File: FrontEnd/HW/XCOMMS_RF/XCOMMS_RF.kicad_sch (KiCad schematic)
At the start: 60 parts, among them J1 SMP-MSLD-PCE-5T, J2 SMP-MSLD-PCE-5T, J3 SFC-110-T2-F-D-A-TR, U1 SIM-14+, U2 HMC788ALP2ETR, U3 HMC952ALP5GE, U5 HMC788ALP2ETR, U6 AD8031, U7 ADT7310, U8 HMC788ALP2ETR

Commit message: XCOMMS Interface rebuild
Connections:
- net +5V renamed Vdd_AMP
- net Vd_PA renamed Vdd_PA
- no-connect marks 0 -> 2
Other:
- note added: "Connectors"
- note added: "Screws"
- note removed: "Alternative 2"
- note removed: "Connectors and Screws"
- note removed: "IC | V (V) | I (mA) | Power (mW) - - - - - - - - - - - - - - - - - - - PA | 6 | 1400 | ~2500 (class C) AMP1 | 5 | 56 | 280 HMC311LP3 AMP2 | 5 | 43 | 21 HMC3587LP3BE VCO | 2.75 | 80 | 220 - - - - - - - - - - - - - - - - - - - Total | 3.2 W Notes: SDR output @ 2 GHz"
- moved on the sheet: C10, C11, C12, C15, C16, C17, C18, C19, C20, C23, C24, C25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

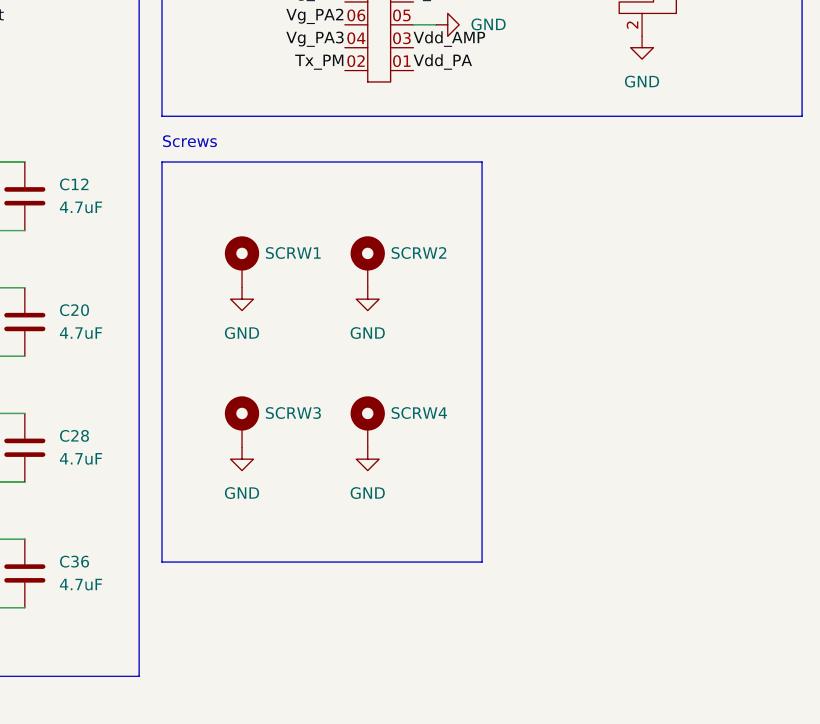
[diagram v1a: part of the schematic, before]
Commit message: xtal changed and routing
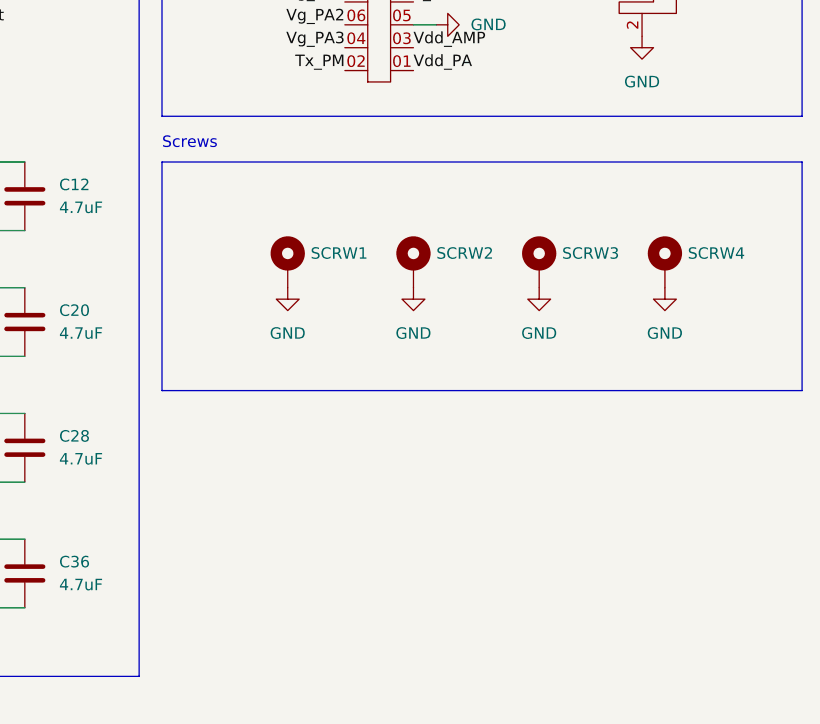
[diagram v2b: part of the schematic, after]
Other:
- moved on the sheet: SCRW1, SCRW2, SCRW3, SCRW4
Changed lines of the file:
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@@
     (stroke (width 0) (type default) (color 0 0 0 0))
   )
-  (polyline (pts (xy 210.82 107.95) (xy 246.38 107.95))
+  (polyline (pts (xy 210.82 107.95) (xy 281.94 107.95))
     (stroke (width 0) (type default) (color 0 0 0 0))
   )
@@
     (stroke (width 0) (type default) (color 0 0 0 0))
   )
-  (polyline (pts (xy 210.82 152.4) (xy 246.38 152.4))
+  (polyline (pts (xy 210.82 133.35) (xy 281.94 133.35))
     (stroke (width 0) (type default) (color 0 0 0 0))
   )
@@
     (stroke (width 0) (type default) (color 0 0 0 0))
   )
-  (polyline (pts (xy 210.82 107.95) (xy 210.82 152.4))
+  (polyline (pts (xy 210.82 107.95) (xy 210.82 133.35))
     (stroke (width 0) (type default) (color 0 0 0 0))
   )
@@
     (stroke (width 0) (type default) (color 0 0 0 0))
   )
-  (polyline (pts (xy 246.38 152.4) (xy 246.38 107.95))
+  (polyline (pts (xy 281.94 133.35) (xy 281.94 107.95))
     (stroke (width 0) (type default) (color 0 0 0 0))
   )
@@
     (pin "1")
   )
-  (symbol (lib_id "Mechanical:MountingHole_Pad") (at 233.68 137.16 0) (unit 1)
+  (symbol (lib_id "Mechanical:MountingHole_Pad") (at 266.7 119.38 0) (unit 1)
     (in_bom yes) (on_board yes) (fields_autoplaced)
-    (property "Reference" "SCRW4" (id 0) (at 236.22 135.8899 0)
+    (property "Reference" "SCRW4" (id 0) (at 269.24 118.1099 0)
       (effects (font (size 1.27 1.27)) (justify left))
     )
-    (property "Value" "MountingHole_Pad" (id 1) (at 233.68 130.81 0)
+    (property "Value" "MountingHole_Pad" (id 1) (at 266.7 113.03 0)
       (effects (font (size 1.27 1.27)) hide)
     )
-    (property "Footprint" "MountingHole:MountingHole_2.7mm_M2.5_ISO14580_Pad" (id 2) (at 233.68 137.16 0)
+    (property "Footprint" "MountingHole:MountingHole_2.7mm_M2.5_ISO14580_Pad" (id 2) (at 266.7 119.38 0)
       (effects (font (size 1.27 1.27)) hide)
     )
-    (property "Datasheet" "~" (id 3) (at 233.68 137.16 0)
+    (property "Datasheet" "~" (id 3) (at 266.7 119.38 0)
       (effects (font (size 1.27 1.27)) hide)
     )
@@
     (pin "2")
   )
-  (symbol (lib_id "power:GND") (at 233.68 139.7 0) (unit 1)
+  (symbol (lib_id "power:GND") (at 266.7 121.92 0) (unit 1)
     (in_bom yes) (on_board yes) (fields_autoplaced)
-    (property "Reference" "#PWR0103" (id 0) (at 233.68 146.05 0)
+    (property "Reference" "#PWR0103" (id 0) (at 266.7 128.27 0)
       (effects (font (size 1.27 1.27)) hide)
     )
-    (property "Value" "GND" (id 1) (at 233.68 144.78 0))
-    (property "Footprint" "" (id 2) (at 233.68 139.7 0)
+    (property "Value" "GND" (id 1) (at 266.7 127 0))
+    (property "Footprint" "" (id 2) (at 266.7 121.92 0)
       (effects (font (size 1.27 1.27)) hide)
     )
-    (property "Datasheet" "" (id 3) (at 233.68 139.7 0)
+    (property "Datasheet" "" (id 3) (at 266.7 121.92 0)
       (effects (font (size 1.27 1.27)) hide)
     )
@@
     (pin "1")
   )
-  (symbol (lib_id "Mechanical:MountingHole_Pad") (at 219.71 137.16 0) (unit 1)
+  (symbol (lib_id "Mechanical:MountingHole_Pad") (at 252.73 119.38 0) (unit 1)
     (in_bom yes) (on_board yes) (fields_autoplaced)
-    (property "Reference" "SCRW3" (id 0) (at 222.25 135.8899 0)
+    (property "Reference" "SCRW3" (id 0) (at 255.27 118.1099 0)
       (effects (font (size 1.27 1.27)) (justify left))
     )
-    (property "Value" "MountingHole_Pad" (id 1) (at 222.25 137.1599 0)
+    (property "Value" "MountingHole_Pad" (id 1) (at 255.27 119.3799 0)
       (effects (font (size 1.27 1.27)) (justify left) hide)
     )
-    (property "Footprint" "MountingHole:MountingHole_2.7mm_M2.5_ISO14580_Pad" (id 2) (at 219.71 137.16 0)
+    (property "Footprint" "MountingHole:MountingHole_2.7mm_M2.5_ISO14580_Pad" (id 2) (at 252.73 119.38 0)
       (effects (font (size 1.27 1.27)) hide)
     )
-    (property "Datasheet" "~" (id 3) (at 219.71 137.16 0)
+    (property "Datasheet" "~" (id 3) (at 252.73 119.38 0)
       (effects (font (size 1.27 1.27)) hide)
     )
@@
     (pin "1")
   )
-  (symbol (lib_id "Mechanical:MountingHole_Pad") (at 233.68 119.38 0) (unit 1)
+  (symbol (lib_id "Mechanical:MountingHole_Pad") (at 238.76 119.38 0) (unit 1)
     (in_bom yes) (on_board yes) (fields_autoplaced)
-    (property "Reference" "SCRW2" (id 0) (at 236.22 118.1099 0)
+    (property "Reference" "SCRW2" (id 0) (at 241.3 118.1099 0)
       (effects (font (size 1.27 1.27)) (justify left))
     )
-    (property "Value" "MountingHole_Pad" (id 1) (at 233.68 113.03 0)
+    (property "Value" "MountingHole_Pad" (id 1) (at 238.76 113.03 0)
       (effects (font (size 1.27 1.27)) hide)
     )
-    (property "Footprint" "MountingHole:MountingHole_2.7mm_M2.5_ISO14580_Pad" (id 2) (at 233.68 119.38 0)
+    (property "Footprint" "MountingHole:MountingHole_2.7mm_M2.5_ISO14580_Pad" (id 2) (at 238.76 119.38 0)
       (effects (font (size 1.27 1.27)) hide)
     )
-    (property "Datasheet" "~" (id 3) (at 233.68 119.38 0)
+    (property "Datasheet" "~" (id 3) (at 238.76 119.38 0)
       (effects (font (size 1.27 1.27)) hide)
     )
@@
     (pin "1")
   )
-  (symbol (lib_id "power:GND") (at 233.68 121.92 0) (unit 1)
+  (symbol (lib_id "power:GND") (at 238.76 121.92 0) (unit 1)
     (in_bom yes) (on_board yes) (fields_autoplaced)
-    (property "Reference" "#PWR0113" (id 0) (at 233.68 128.27 0)
+    (property "Reference" "#PWR0113" (id 0) (at 238.76 128.27 0)
       (effects (font (size 1.27 1.27)) hide)
     )
-    (property "Value" "GND" (id 1) (at 233.68 127 0))
-    (property "Footprint" "" (id 2) (at 233.68 121.92 0)
+    (property "Value" "GND" (id 1) (at 238.76 127 0))
+    (property "Footprint" "" (id 2) (at 238.76 121.92 0)
       (effects (font (size 1.27 1.27)) hide)
     )
-    (property "Datasheet" "" (id 3) (at 233.68 121.92 0)
+    (property "Datasheet" "" (id 3) (at 238.76 121.92 0)
       (effects (font (size 1.27 1.27)) hide)
     )
@@
     (pin "2")
   )
-  (symbol (lib_id "Mechanical:MountingHole_Pad") (at 219.71 119.38 0) (unit 1)
+  (symbol (lib_id "Mechanical:MountingHole_Pad") (at 224.79 119.38 0) (unit 1)
     (in_bom yes) (on_board yes) (fields_autoplaced)
-    (property "Reference" "SCRW1" (id 0) (at 222.25 118.1099 0)
+    (property "Reference" "SCRW1" (id 0) (at 227.33 118.1099 0)
       (effects (font (size 1.27 1.27)) (justify left))
     )
-    (property "Value" "MountingHole_Pad" (id 1) (at 222.25 119.3799 0)
+    (property "Value" "MountingHole_Pad" (id 1) (at 227.33 119.3799 0)
       (effects (font (size 1.27 1.27)) (justify left) hide)
     )
-    (property "Footprint" "MountingHole:MountingHole_2.7mm_M2.5_ISO14580_Pad" (id 2) (at 219.71 119.38 0)
+    (property "Footprint" "MountingHole:MountingHole_2.7mm_M2.5_ISO14580_Pad" (id 2) (at 224.79 119.38 0)
       (effects (font (size 1.27 1.27)) hide)
     )
-    (property "Datasheet" "~" (id 3) (at 219.71 119.38 0)
+    (property "Datasheet" "~" (id 3) (at 224.79 119.38 0)
       (effects (font (size 1.27 1.27)) hide)
     )
@@
     (pin "1")
   )
-  (symbol (lib_id "power:GND") (at 219.71 121.92 0) (unit 1)
+  (symbol (lib_id "power:GND") (at 224.79 121.92 0) (unit 1)
     (in_bom yes) (on_board yes) (fields_autoplaced)
-    (property "Reference" "#PWR0114" (id 0) (at 219.71 128.27 0)
+    (property "Reference" "#PWR0114" (id 0) (at 224.79 128.27 0)
       (effects (font (size 1.27 1.27)) hide)
     )
-    (property "Value" "GND" (id 1) (at 219.71 127 0))
-    (property "Footprint" "" (id 2) (at 219.71 121.92 0)
+    (property "Value" "GND" (id 1) (at 224.79 127 0))
+    (property "Footprint" "" (id 2) (at 224.79 121.92 0)
       (effects (font (size 1.27 1.27)) hide)
     )
-    (property "Datasheet" "" (id 3) (at 219.71 121.92 0)
+    (property "Datasheet" "" (id 3) (at 224.79 121.92 0)
       (effects (font (size 1.27 1.27)) hide)
     )
@@
     (pin "1")
   )
-  (symbol (lib_id "power:GND") (at 219.71 139.7 0) (unit 1)
+  (symbol (lib_id "power:GND") (at 252.73 121.92 0) (unit 1)
     (in_bom yes) (on_board yes) (fields_autoplaced)
-    (property "Reference" "#PWR0106" (id 0) (at 219.71 146.05 0)
+    (property "Reference" "#PWR0106" (id 0) (at 252.73 128.27 0)
       (effects (font (size 1.27 1.27)) hide)
     )
-    (property "Value" "GND" (id 1) (at 219.71 144.78 0))
-    (property "Footprint" "" (id 2) (at 219.71 139.7 0)
+    (property "Value" "GND" (id 1) (at 252.73 127 0))
+    (property "Footprint" "" (id 2) (at 252.73 121.92 0)
       (effects (font (size 1.27 1.27)) hide)
     )
-    (property "Datasheet" "" (id 3) (at 219.71 139.7 0)
+    (property "Datasheet" "" (id 3) (at 252.73 121.92 0)
       (effects (font (size 1.27 1.27)) hide)
     )

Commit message: XCOMMS RF
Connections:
- net GND: now also J3.08; no longer J3.18, J3.20
- net SCK: now also J3.17; no longer J3.15
- net SDI: now also J3.20; no longer J3.19
- net SDO: now also J3.19; no longer J3.17
- net Tx_PM: now also J3.18; no longer J3.02
- net Vg_PA1: now also J3.06; no longer J3.08
- net Vg_PA2: now also J3.04; no longer J3.06
- net Vg_PA3: now also J3.02; no longer J3.04
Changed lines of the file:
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@@
   (junction (at 96.52 143.51) (diameter 0) (color 0 0 0 0)
   )
-  (junction (at 231.14 80.01) (diameter 0) (color 0 0 0 0)
-  )
   (junction (at 49.53 33.02) (diameter 0) (color 0 0 0 0)
   )
@@
   )
   (junction (at 26.67 33.02) (diameter 0) (color 0 0 0 0)
-  )
-  (junction (at 231.14 77.47) (diameter 0) (color 0 0 0 0)
   )
   (junction (at 182.88 107.95) (diameter 0) (color 0 0 0 0)
@@
     (stroke (width 0) (type default) (color 0 0 0 0))
   )
-  (wire (pts (xy 231.14 77.47) (xy 231.14 80.01))
-    (stroke (width 0) (type default) (color 0 0 0 0))
-  )
   (wire (pts (xy 241.3 92.71) (xy 238.76 92.71))
     (stroke (width 0) (type default) (color 0 0 0 0))
@@
     (stroke (width 0) (type default) (color 0 0 0 0))
   )
+  (wire (pts (xy 231.14 87.63) (xy 231.14 90.17))
+    (stroke (width 0) (type default) (color 0 0 0 0))
+  )
   (wire (pts (xy 109.22 41.91) (xy 109.22 39.37))
     (stroke (width 0) (type default) (color 0 0 0 0))
   )
   (wire (pts (xy 252.73 73.66) (xy 259.08 73.66))
-    (stroke (width 0) (type default) (color 0 0 0 0))
-  )
-  (wire (pts (xy 231.14 74.93) (xy 231.14 77.47))
     (stroke (width 0) (type default) (color 0 0 0 0))
   )
@@
     (effects (font (size 1.27 1.27)) (justify left bottom))
   )
-  (label "SDI" (at 238.76 74.93 0)
-    (effects (font (size 1.27 1.27)) (justify left bottom))
-  )
   (label "Vdd_AMP" (at 223.52 45.72 0)
     (effects (font (size 1.27 1.27)) (justify left bottom))
@@
     (effects (font (size 1.27 1.27)) (justify left bottom))
   )
-  (label "Vg_PA3" (at 231.14 95.25 180)
+  (label "RF_In" (at 19.05 27.94 0)
+    (effects (font (size 1.27 1.27)) (justify left bottom))
+  )
+  (label "PLL_CSB" (at 21.59 86.36 0)
+    (effects (font (size 1.27 1.27)) (justify left bottom))
+  )
+  (label "Vdd_PA" (at 158.75 73.66 90)
+    (effects (font (size 1.27 1.27)) (justify left bottom))
+  )
+  (label "SDO" (at 238.76 74.93 0)
+    (effects (font (size 1.27 1.27)) (justify left bottom))
+  )
+  (label "RF_out" (at 189.23 88.9 0)
+    (effects (font (size 1.27 1.27)) (justify left bottom))
+  )
+  (label "Vdd_PA" (at 163.83 73.66 90)
+    (effects (font (size 1.27 1.27)) (justify left bottom))
+  )
+  (label "Vdet" (at 189.23 92.71 0)
+    (effects (font (size 1.27 1.27)) (justify left bottom))
+  )
+  (label "PLL_CE" (at 238.76 87.63 0)
+    (effects (font (size 1.27 1.27)) (justify left bottom))
+  )
+  (label "Vg_PA2" (at 172.72 73.66 90)
+    (effects (font (size 1.27 1.27)) (justify left bottom))
+  )
+  (label "FL_Out" (at 151.13 31.75 0)
+    (effects (font (size 1.27 1.27)) (justify left bottom))
+  )
+  (label "PLL_CSB" (at 238.76 82.55 0)
+    (effects (font (size 1.27 1.27)) (justify left bottom))
+  )
+  (label "Vdd_PA" (at 166.37 73.66 90)
+    (effects (font (size 1.27 1.27)) (justify left bottom))
+  )
+  (label "AMP3_Out" (at 78.74 76.2 0)
+    (effects (font (size 1.27 1.27)) (justify left bottom))
+  )
+  (label "Vdd_PA" (at 172.72 107.95 0)
+    (effects (font (size 1.27 1.27)) (justify left bottom))
+  )
+  (label "PA_RF_IN" (at 137.16 88.9 0)
+    (effects (font (size 1.27 1.27)) (justify left bottom))
+  )
+  (label "AMP2_Out" (at 232.41 27.94 0)
+    (effects (font (size 1.27 1.27)) (justify left bottom))
+  )
+  (label "Vdd_AMP" (at 73.66 125.73 0)
+    (effects (font (size 1.27 1.27)) (justify left bottom))
+  )
+  (label "Vdd_AMP" (at 86.36 125.73 0)
+    (effects (font (size 1.27 1.27)) (justify left bottom))
+  )
+  (label "SCK" (at 238.76 77.47 0)
+    (effects (font (size 1.27 1.27)) (justify left bottom))
+  )
+  (label "Vg_PA3" (at 231.14 97.79 180)
     (effects (font (size 1.27 1.27)) (justify right bottom))
   )
-  (label "RF_In" (at 19.05 27.94 0)
-    (effects (font (size 1.27 1.27)) (justify left bottom))
-  )
-  (label "PLL_CSB" (at 21.59 86.36 0)
-    (effects (font (size 1.27 1.27)) (justify left bottom))
-  )
-  (label "Vdd_PA" (at 158.75 73.66 90)
-    (effects (font (size 1.27 1.27)) (justify left bottom))
-  )
-  (label "RF_out" (at 189.23 88.9 0)
-    (effects (font (size 1.27 1.27)) (justify left bottom))
-  )
-  (label "Vdd_PA" (at 163.83 73.66 90)
-    (effects (font (size 1.27 1.27)) (justify left bottom))
-  )
-  (label "Vdet" (at 189.23 92.71 0)
-    (effects (font (size 1.27 1.27)) (justify left bottom))
-  )
-  (label "PLL_CE" (at 238.76 87.63 0)
-    (effects (font (size 1.27 1.27)) (justify left bottom))
-  )
-  (label "Vg_PA2" (at 172.72 73.66 90)
-    (effects (font (size 1.27 1.27)) (justify left bottom))
-  )
-  (label "FL_Out" (at 151.13 31.75 0)
-    (effects (font (size 1.27 1.27)) (justify left bottom))
-  )
-  (label "PLL_CSB" (at 238.76 82.55 0)
-    (effects (font (size 1.27 1.27)) (justify left bottom))
-  )
-  (label "Vdd_PA" (at 166.37 73.66 90)
-    (effects (font (size 1.27 1.27)) (justify left bottom))
-  )
-  (label "AMP3_Out" (at 78.74 76.2 0)
-    (effects (font (size 1.27 1.27)) (justify left bottom))
-  )
-  (label "Vdd_PA" (at 172.72 107.95 0)
-    (effects (font (size 1.27 1.27)) (justify left bottom))
-  )
-  (label "PA_RF_IN" (at 137.16 88.9 0)
-    (effects (font (size 1.27 1.27)) (justify left bottom))
-  )
-  (label "AMP2_Out" (at 232.41 27.94 0)
-    (effects (font (size 1.27 1.27)) (justify left bottom))
-  )
-  (label "Vdd_AMP" (at 73.66 125.73 0)
-    (effects (font (size 1.27 1.27)) (justify left bottom))
-  )
-  (label "Vdd_AMP" (at 86.36 125.73 0)
-    (effects (font (size 1.27 1.27)) (justify left bottom))
+  (label "Tx_PM" (at 231.14 77.47 180)
+    (effects (font (size 1.27 1.27)) (justify right bottom))
   )
   (label "Vg_PA1" (at 170.18 73.66 90)
@@
     (effects (font (size 1.27 1.27)) (justify left bottom))
   )
-  (label "Tx_PM" (at 231.14 97.79 180)
+  (label "SDI" (at 231.14 74.93 180)
     (effects (font (size 1.27 1.27)) (justify right bottom))
   )
-  (label "Vg_PA1" (at 231.14 90.17 180)
+  (label "Vg_PA1" (at 231.14 92.71 180)
     (effects (font (size 1.27 1.27)) (justify right bottom))
   )
@@
     (effects (font (size 1.27 1.27)) (justify left bottom))
   )
-  (label "SCK" (at 238.76 80.01 0)
-    (effects (font (size 1.27 1.27)) (justify left bottom))
-  )
   (label "RF_out" (at 252.73 73.66 0)
     (effects (font (size 1.27 1.27)) (justify left bottom))
@@
     (effects (font (size 1.27 1.27)) (justify left bottom))
   )
-  (label "SDO" (at 238.76 77.47 0)
-    (effects (font (size 1.27 1.27)) (justify left bottom))
-  )
   (label "Vdd_AMP" (at 238.76 95.25 0)
     (effects (font (size 1.27 1.27)) (justify left bottom))
@@
     (effects (font (size 1.27 1.27)) (justify left bottom))
   )
-  (label "Vg_PA2" (at 231.14 92.71 180)
+  (label "Vg_PA2" (at 231.14 95.25 180)
     (effects (font (size 1.27 1.27)) (justify right bottom))
   )
